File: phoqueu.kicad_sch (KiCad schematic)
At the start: 50 parts, among them J1 18…56 V, J2 MCU bypass, J3 Voltage select, J4 3.3…24 V, Q1 NX138AK, U1 i7A4W033A033V, U2 TMCS1108A1U, U3 TMCS1108A1U

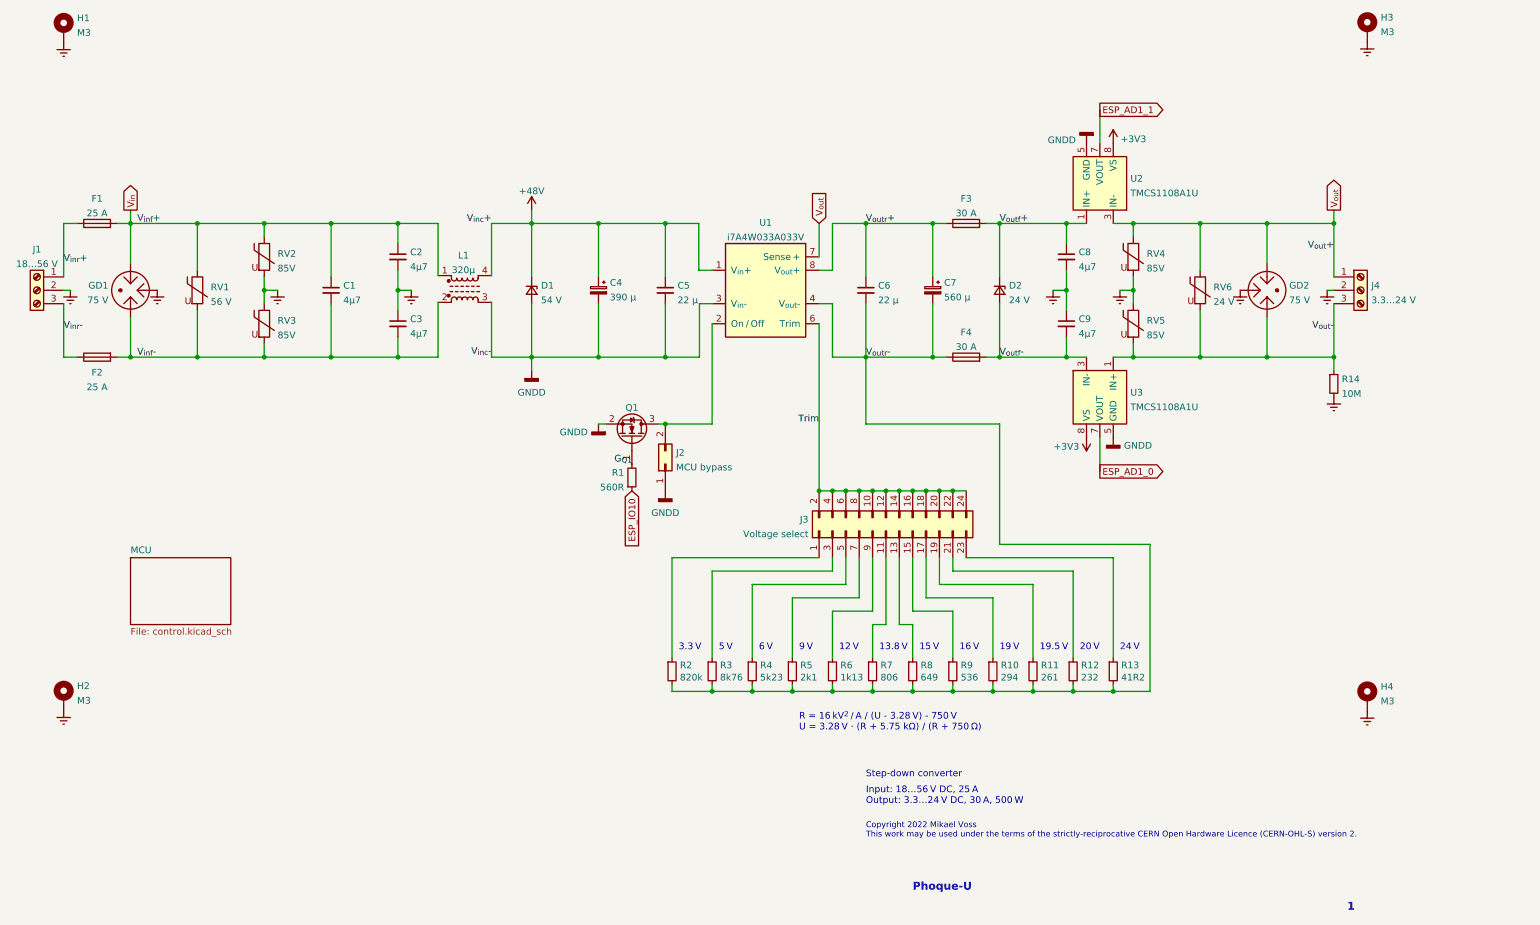
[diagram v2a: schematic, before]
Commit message: Complete placement and routeing
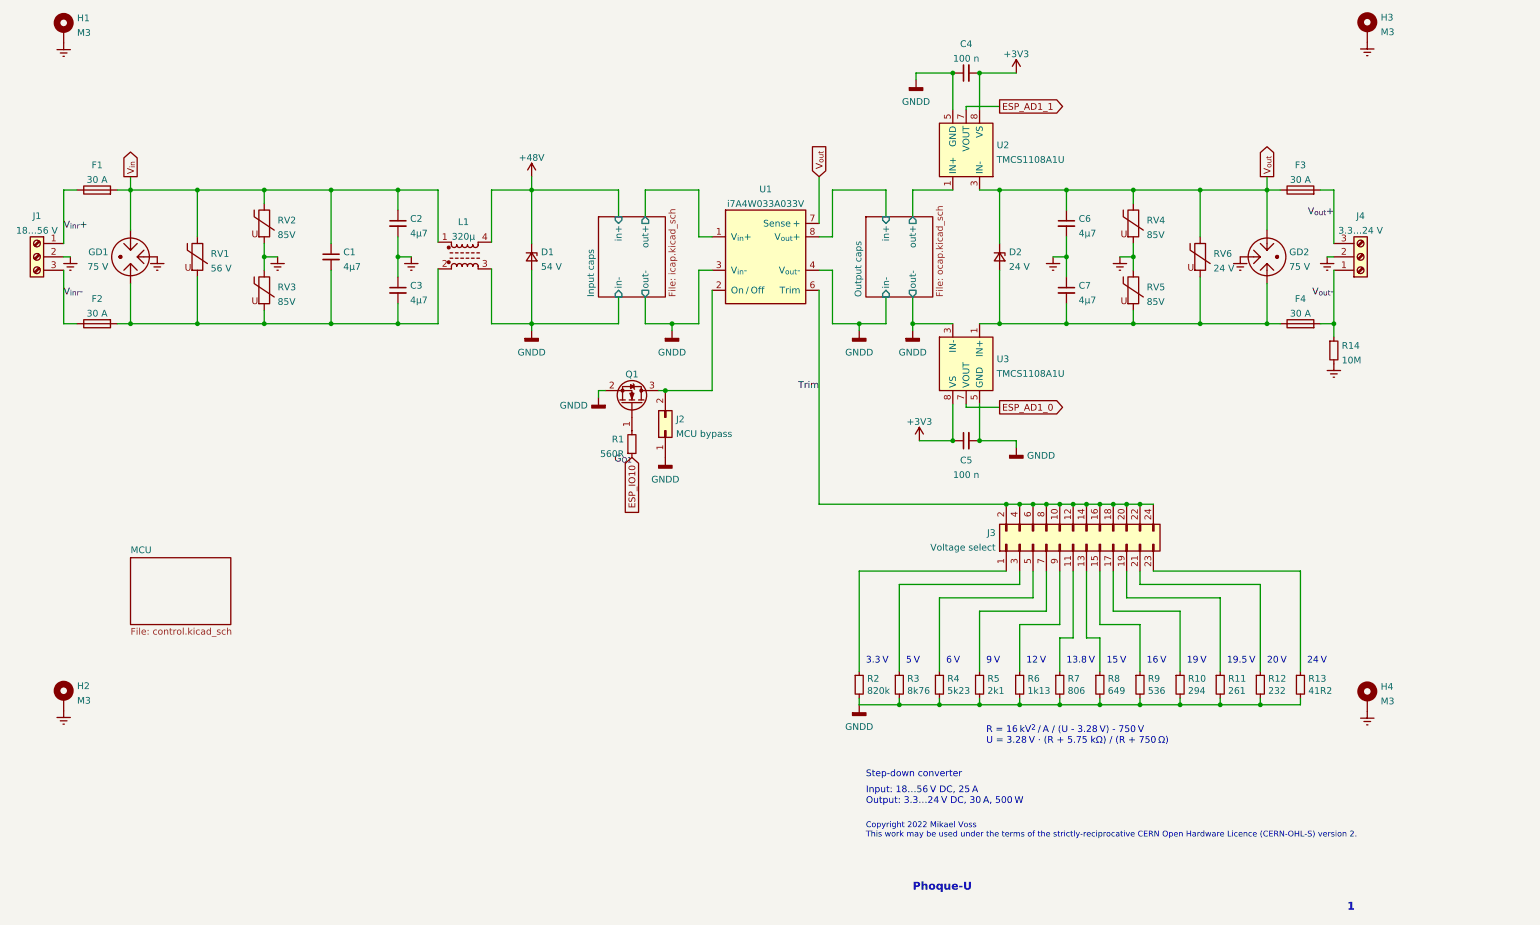
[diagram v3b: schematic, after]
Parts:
- removed C4: 390 µ, Capacitor_THT:CP_Radial_D12.5mm_P5.00mm, symbol Device:C_Polarized_Small
- removed C6: 22 µ, Capacitor_SMD:C_2220_5650Metric, symbol Device:C_Small
- removed C7: 560 µ, Capacitor_THT:CP_Radial_D10.0mm_P5.00mm, symbol Device:C_Polarized_Small
- added C4: 100 n, Capacitor_SMD:C_0402_1005Metric, symbol Device:C_Small
- C5: value 22 µ -> 100 n; footprint Capacitor_SMD:C_2220_5650Metric -> Capacitor_SMD:C_0402_1005Metric; Manufacturer Murata -> (none); Part Number KRM55WR72A226MH01L -> (none)
- F1: value 25 A -> 30 A; footprint phq_THT:Keystone_3557 -> phq_SMD:Fuse_2410_20A; Manufacturer (none) -> Eaton; Part Number 3557 -> CB61F30A
- F2: value 25 A -> 30 A; footprint phq_THT:Keystone_3557 -> phq_SMD:Fuse_2410_20A; Manufacturer (none) -> Eaton; Part Number (none) -> CB61F30A
- F3, F4: footprint phq_THT:Keystone_3557 -> phq_SMD:Fuse_2410_20A; Manufacturer (none) -> Eaton; Part Number 3557 -> CB61F30A
- J2: footprint Connector_PinHeader_2.54mm:PinHeader_2x01_P2.54mm_Vertical -> Connector_PinHeader_2.00mm:PinHeader_2x01_P2.00mm_Vertical
- J3: footprint Connector_PinHeader_2.54mm:PinHeader_2x12_P2.54mm_Vertical -> Connector_PinHeader_2.00mm:PinHeader_2x12_P2.00mm_Vertical
- R1, R10, R11, R12, R13, R14, R2, R3, R4, R5, R6, R7, R8, R9: footprint Resistor_SMD:R_0805_2012Metric -> Resistor_SMD:R_0603_1608Metric
- renumbered C8 to C6, C9 to C7
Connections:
- net +3V3: now also C5.1, C4.2
- net +48V: no longer C5.1, U1.1 (V_{in}+)
- net GNDD: now also R10.2, R11.2, R12.2, R13.2, R2.2, R3.2, R4.2, R5.2, R6.2, R7.2, R8.2, R9.2, U1.4 (V_{out}-), U3.3 (IN-), U3.4 (IN-), C4.1
- net G_{Q1}: no longer Q1.1 (G), R1.2
- net V_{out}: now also C6.1, D2.1 (K), F3.1; no longer J4.1 (Pin_1)
- net V_{out}-: now also F4.2, J4.1 (Pin_1); no longer GD2.1, J4.3 (Pin_3), RV5.2, RV6.2, U3.1 (IN+), U3.2 (IN+)
- net V_{inf}-: no longer names the net of C1.2, C3.2, F2.2, GD1.3, L1.2, RV1.2, RV3.2
- removed net V_{outf}+: C6.1, D2.1 (K), F3.2, U2.1 (IN+), U2.2 (IN+)
- removed net V_{outf}-: C7.2, D2.2 (A), F4.2, U3.3 (IN-), U3.4 (IN-)
- net V_{outr}+ renamed Output caps/in+
- net Output caps/in+: no longer F3.1
- removed net V_{outr}-: F4.1, R10.2, R11.2, R12.2, R13.2, R2.2, R3.2, R4.2, R5.2, R6.2, R7.2, R8.2, R9.2, U1.4 (V_{out}-)
- new net: C7.2, D2.2 (A), F4.1, GD2.1, RV5.2, RV6.2, U3.1 (IN+), U3.2 (IN+)
- new net: Q1.1 (G), R1.2
- new net Input caps/out+: U1.1 (V_{in}+)
- new net Output caps/out+: U2.1 (IN+), U2.2 (IN+)
- new net V_{out}+: F3.2, J4.3 (Pin_3)
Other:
- added sheet Input caps (icap.kicad_sch)
- added sheet Output caps (ocap.kicad_sch)
- moved on the sheet: C1, C2, C3, C6, C7, D1, D2, F1, F2, GD1, GD2, J1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
